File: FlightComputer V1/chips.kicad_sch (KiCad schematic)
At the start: 8 parts, among them Q1 IRLZ44N, Q2 IRLZ44N, U1 BMP280, U2 MPU-6050, U3 W25Q64, U4 GY-BMP280, U5 Micro-SD-Card-Holder

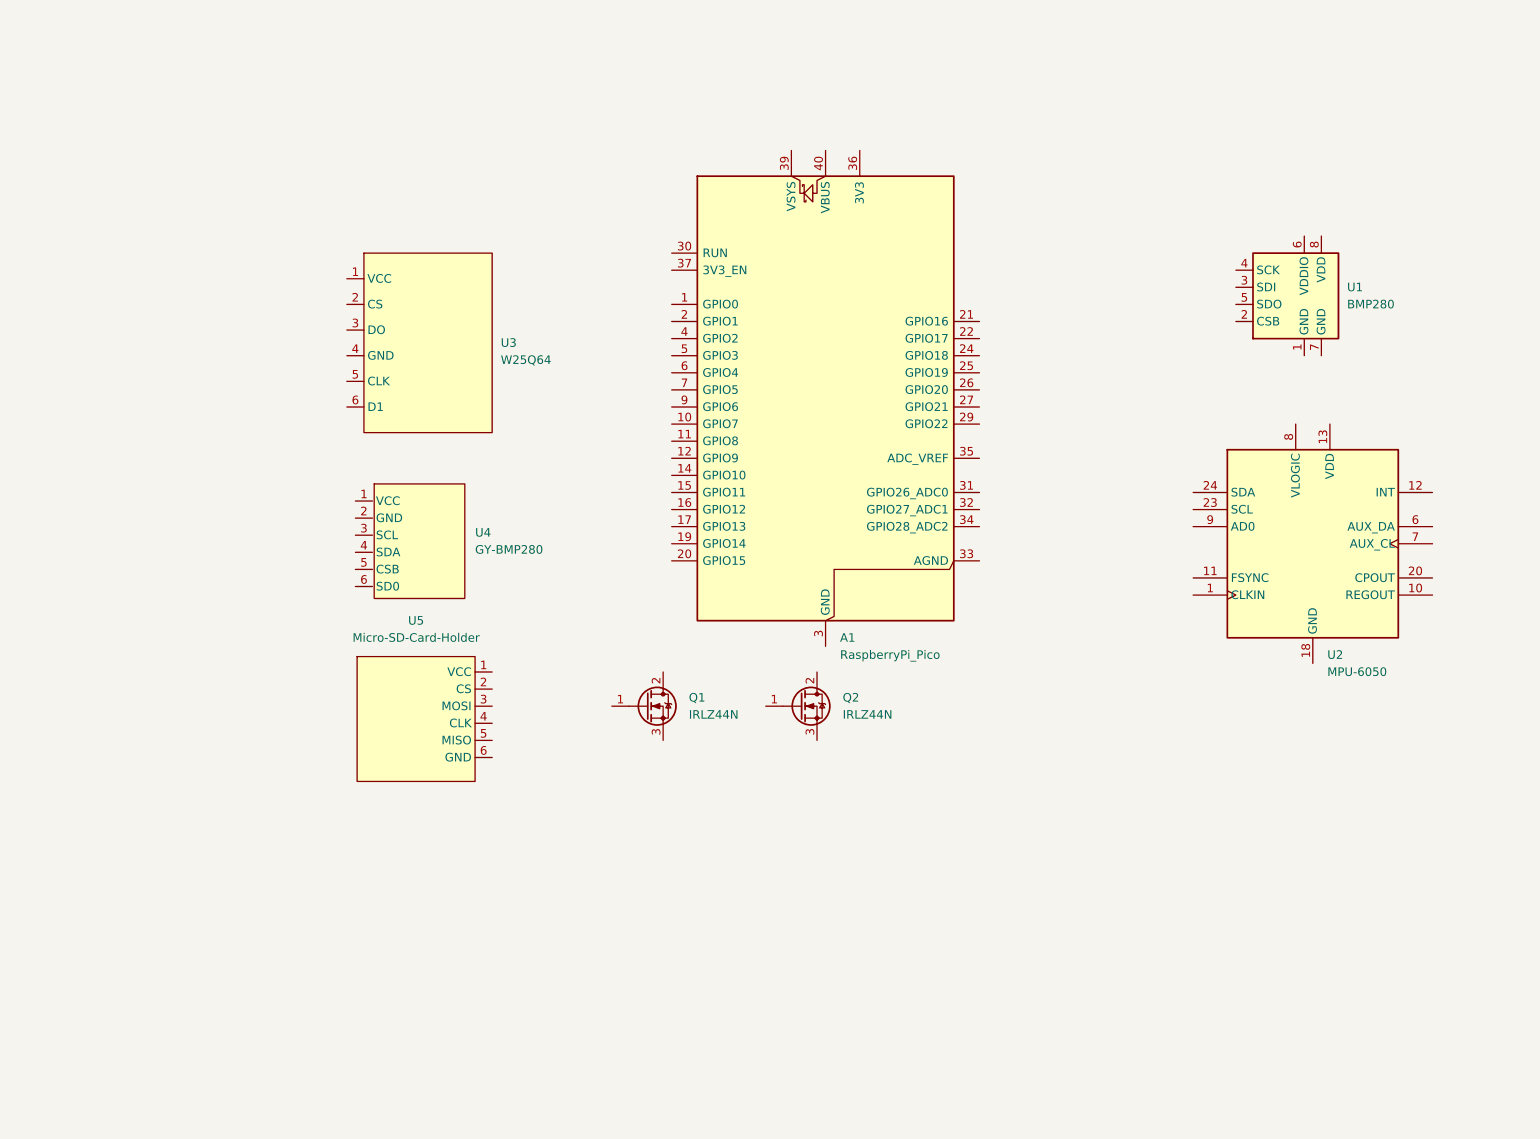
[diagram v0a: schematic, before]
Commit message: pin connection
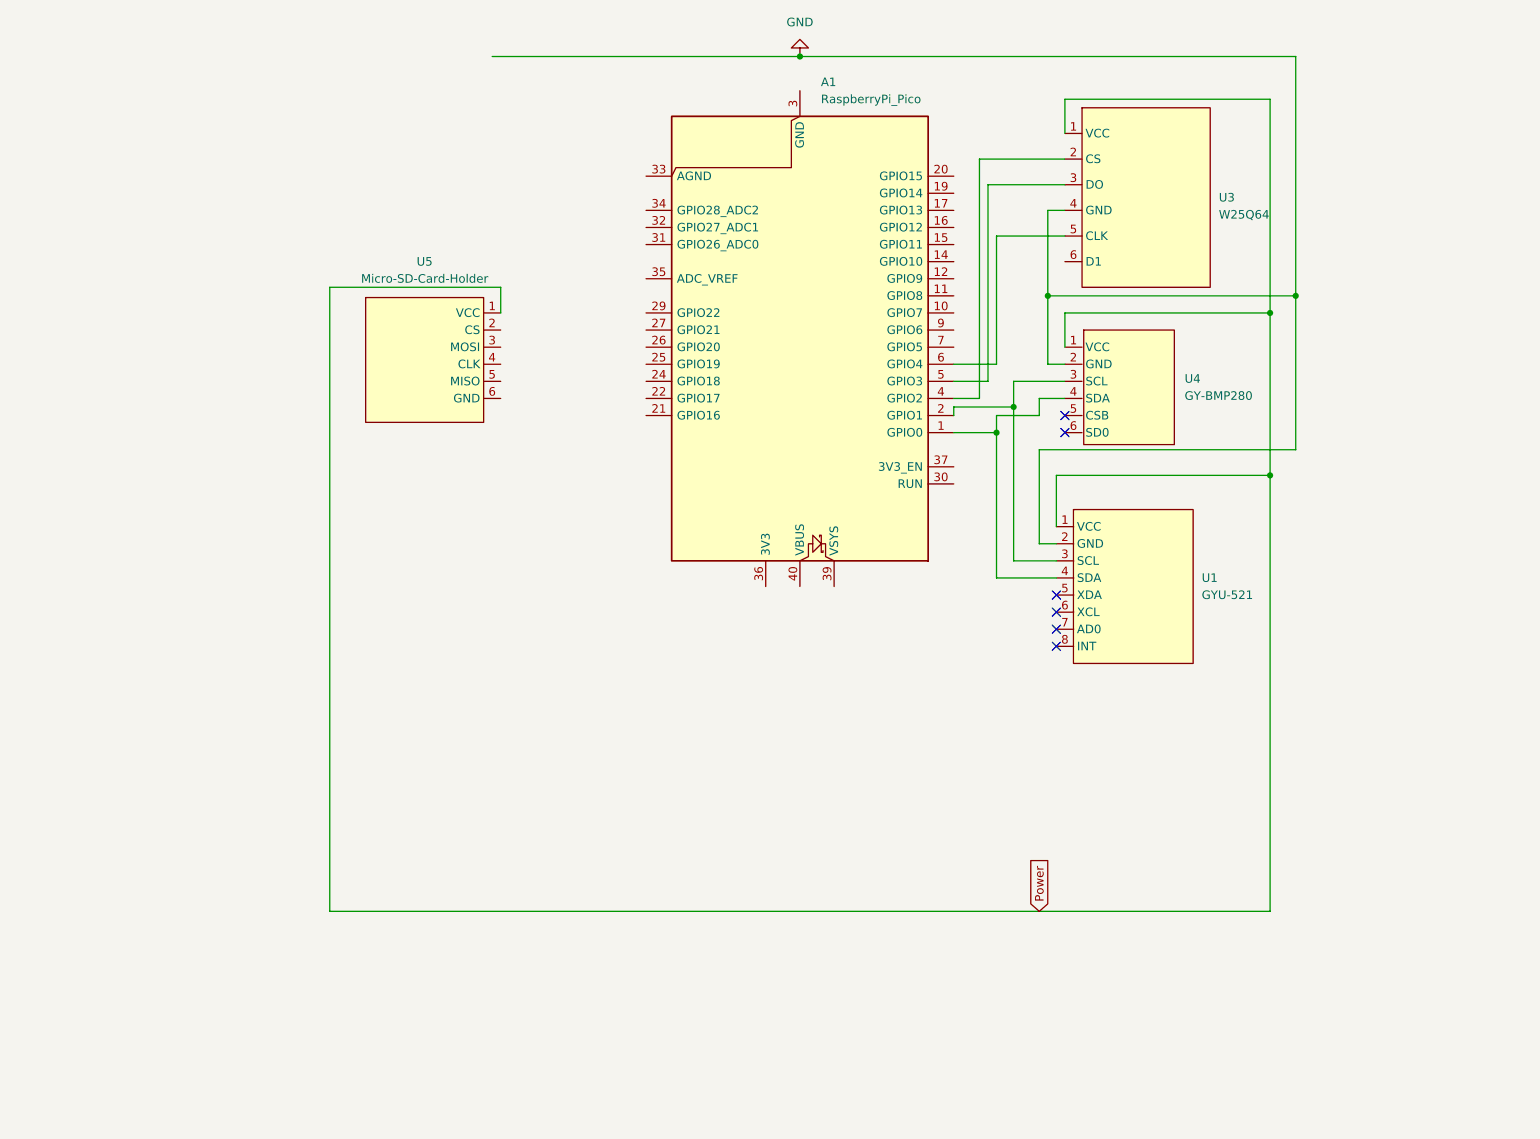
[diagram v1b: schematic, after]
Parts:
- removed Q1, Q2: IRLZ44N, Package_TO_SOT_THT:TO-220-3_Vertical, symbol Transistor_FET:IRLZ44N
- removed U1: BMP280, Package_LGA:Bosch_LGA-8_2x2.5mm_P0.65mm_ClockwisePinNumbering, symbol Sensor_Pressure:BMP280
- removed U2: MPU-6050, Sensor_Motion:InvenSense_QFN-24_4x4mm_P0.5mm, symbol Sensor_Motion:MPU-6050
- added U1: GYU-521, symbol FlightComputerV1Parts:GY-521_MPU6050
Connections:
- net Power: now reaches U5.1 (VCC)
- net Power: now also U3.1 (VCC), U4.1 (VCC), U1.1 (VCC)
- net at U3.2 (CS): now also A1.4 (GPIO2)
- net at U3.3 (DO): now also A1.5 (GPIO3)
- net GND: now reaches U3.4 (GND)
- net GND: now also U4.2 (GND), U1.2 (GND)
- net at U3.5 (CLK): now also A1.6 (GPIO4)
- net at U4.3 (SCL): now also A1.2 (GPIO1), U1.3 (SCL)
- net at U4.4 (SDA): now also A1.1 (GPIO0), U1.4 (SDA)
- no-connect marks 0 -> 6
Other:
- moved on the sheet: A1, U3, U4, U5

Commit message: All chip pins connected
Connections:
- net GND: now also U5.6 (GND)
- net at U5.2 (CS): now also A1.27 (GPIO21)
- net at U5.3 (MOSI): now also A1.25 (GPIO19)
- net at U5.4 (CLK): now also A1.24 (GPIO18)
- net at U5.5 (MISO): now also A1.21 (GPIO16)
- net at U3.2 (CS): now also A1.7 (GPIO5); no longer A1.4 (GPIO2)
- net at U3.3 (DO): now also A1.6 (GPIO4); no longer A1.5 (GPIO3)
- net at U3.5 (CLK): now also A1.4 (GPIO2); no longer A1.6 (GPIO4)
- net at U3.6 (D1): now also A1.11 (GPIO8)

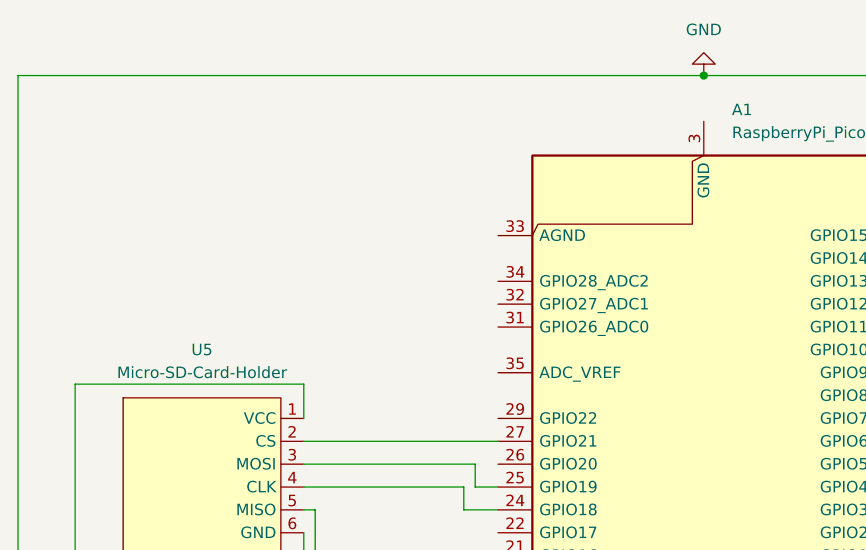
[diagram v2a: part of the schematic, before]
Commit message: forgot to connect the pico to power oops
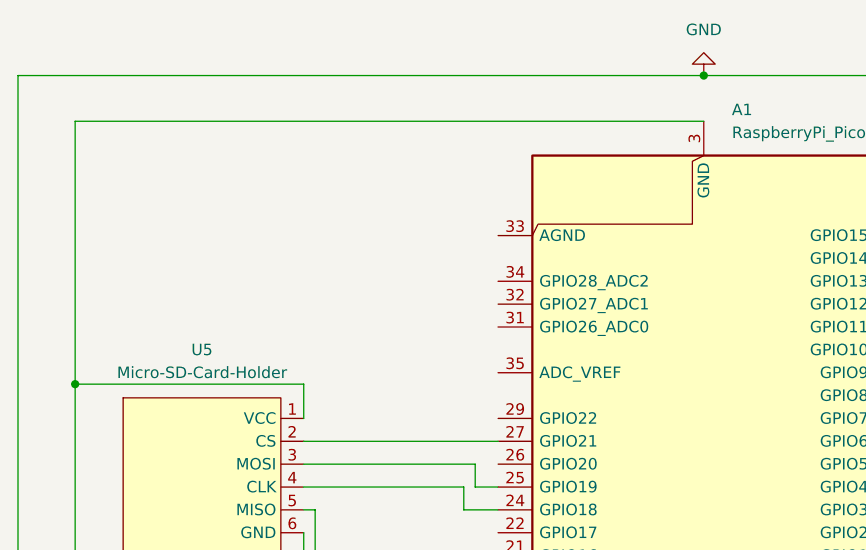
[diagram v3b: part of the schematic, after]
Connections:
- net Power: now also A1.13 (GND), A1.18 (GND), A1.23 (GND), A1.28 (GND), A1.3 (GND), A1.38 (GND), A1.8 (GND)
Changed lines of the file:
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@@
+	)
+	(junction
+		(at 73.66 59.69)
+		(diameter 0)
+		(color 0 0 0 0)
 	)
 	(junction
@@
 			(width 0)
 			(type default)
+			(color 255 0 0 1)
 		)
 	)
@@
 	(wire
 		(pts
+			(xy 73.66 30.48) (xy 73.66 59.69)
+		)
+		(stroke
+			(width 0)
+			(type default)
+			(color 255 0 0 1)
+		)
+	)
+	(wire
+		(pts
 			(xy 182.88 55.88) (xy 167.64 55.88)
 		)
@@
 		)
 	)
+	(wire
+		(pts
+			(xy 143.51 30.48) (xy 73.66 30.48)
+		)
+		(stroke
+			(width 0)
+			(type default)
+			(color 255 0 0 1)
+		)
+	)

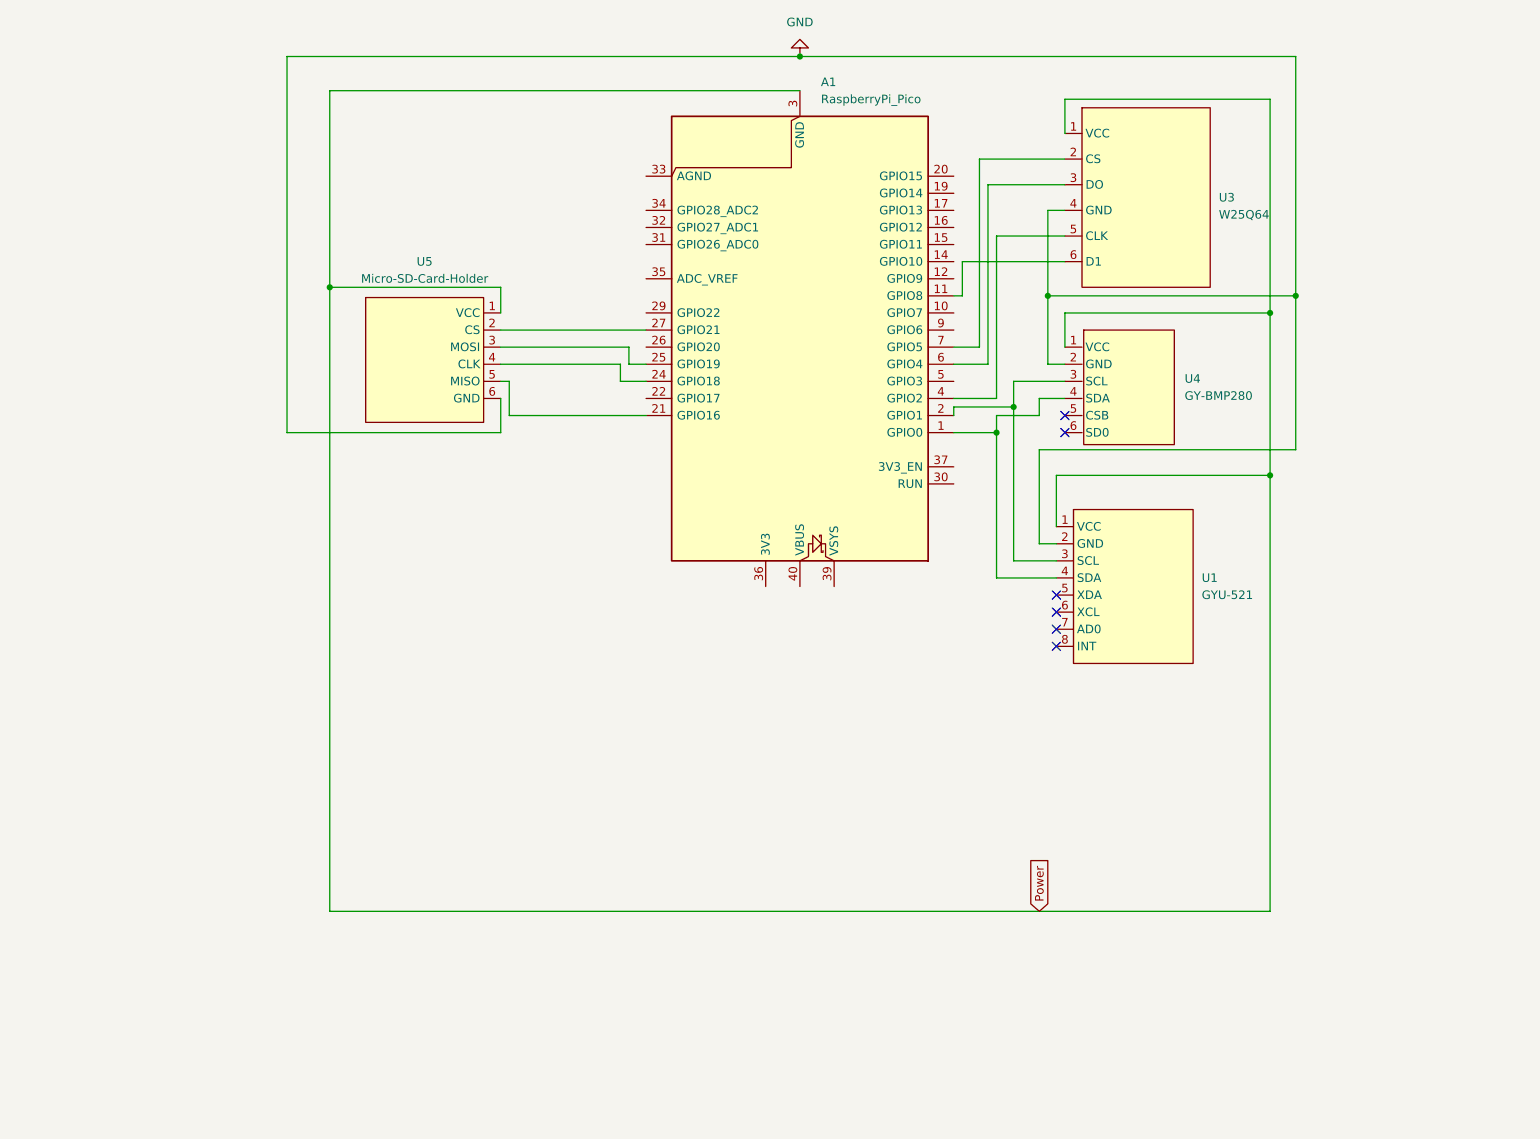
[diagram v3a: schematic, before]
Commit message: Reconnected to have SPI based chips to be connected to the same bus
connected to SPI0 not SPI11
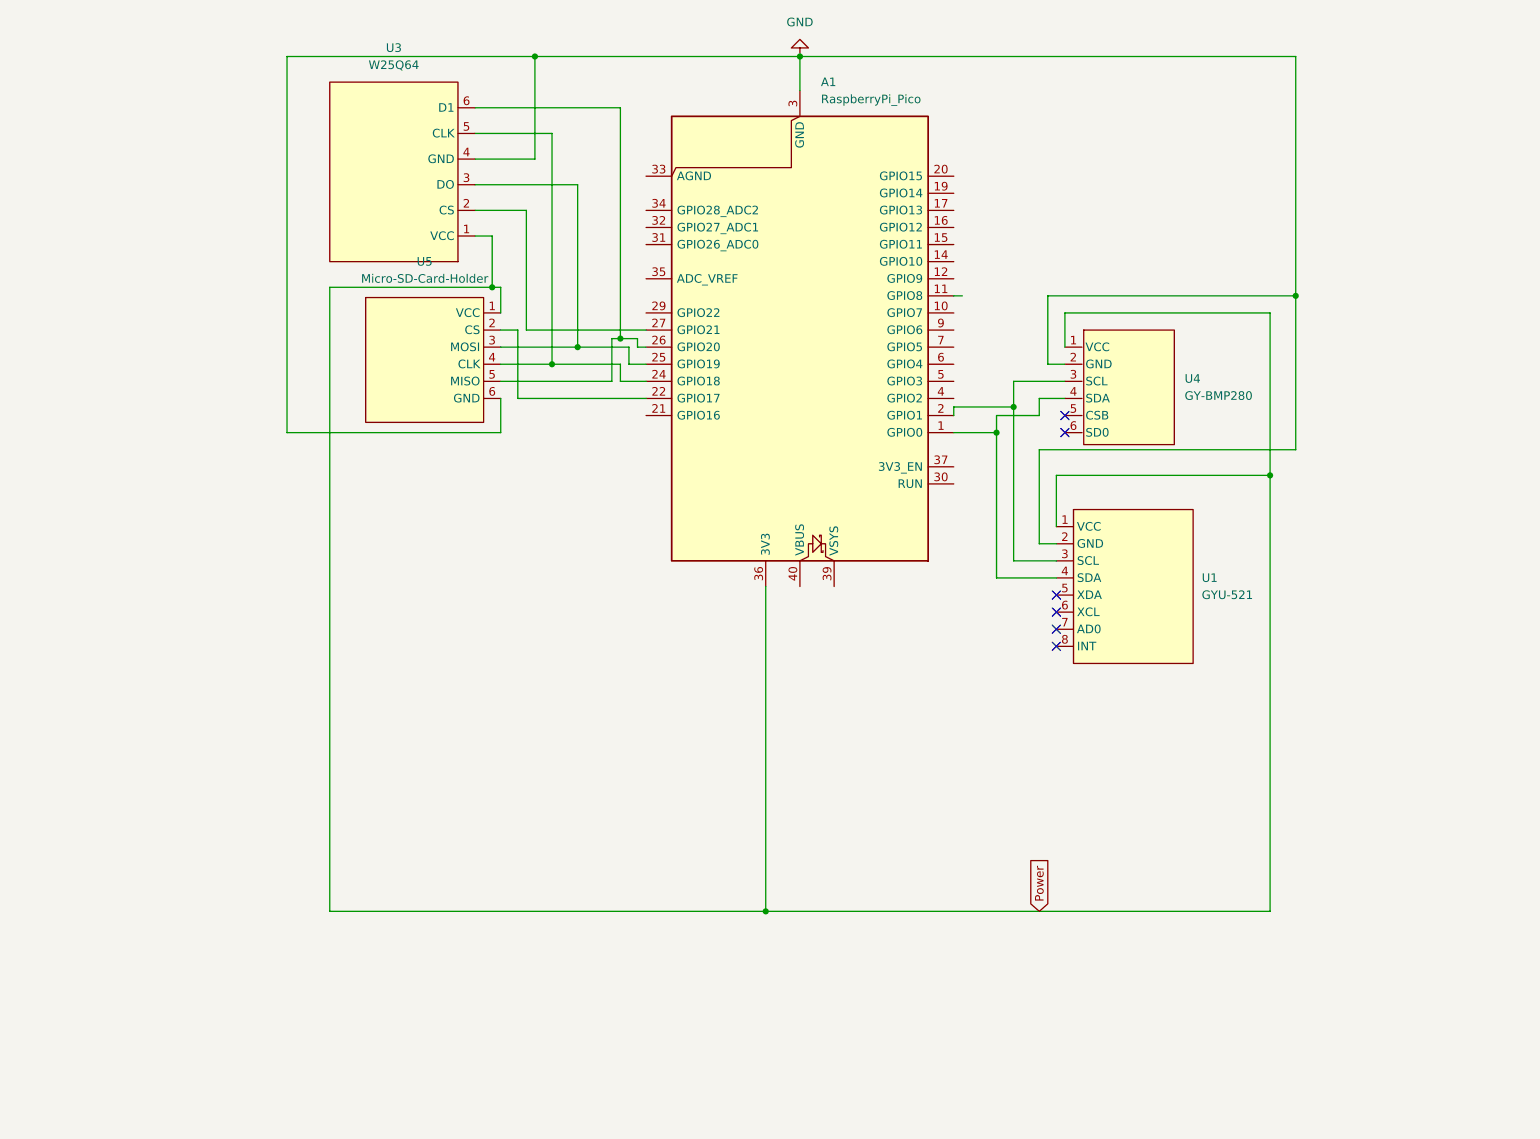
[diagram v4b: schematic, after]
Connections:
- net GND: now also A1.13 (GND), A1.18 (GND), A1.23 (GND), A1.28 (GND), A1.3 (GND), A1.38 (GND), A1.8 (GND)
- net Power: now also A1.36 (3V3); no longer A1.13 (GND), A1.18 (GND), A1.23 (GND), A1.28 (GND), A1.3 (GND), A1.38 (GND), A1.8 (GND)
- net at U5.2 (CS): now also A1.22 (GPIO17); no longer A1.27 (GPIO21)
- net at A1.25 (GPIO19), U5.3 (MOSI): now also U3.3 (DO)
- net at A1.24 (GPIO18), U5.4 (CLK): now also U3.5 (CLK)
- net at U5.5 (MISO): now also A1.26 (GPIO20), U3.6 (D1); no longer A1.21 (GPIO16)
- net at U3.2 (CS): now also A1.27 (GPIO21); no longer A1.7 (GPIO5)
- net at A1.6 (GPIO4): no longer U3.3 (DO)
- net at A1.4 (GPIO2): no longer U3.5 (CLK)
- net at A1.11 (GPIO8): no longer U3.6 (D1)
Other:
- moved on the sheet: U3
